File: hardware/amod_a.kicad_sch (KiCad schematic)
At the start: 50 parts, among them J101 USB-C, J102 rails, J201 SMA, J202 SMA, J301 SMA, J302 SMA, Q201 AO3401A, Q301 AO3401A, SW201 ON, SW301 ON, U101 LM2664, U102 3.3V, U201 OPA810, U301 OPA810

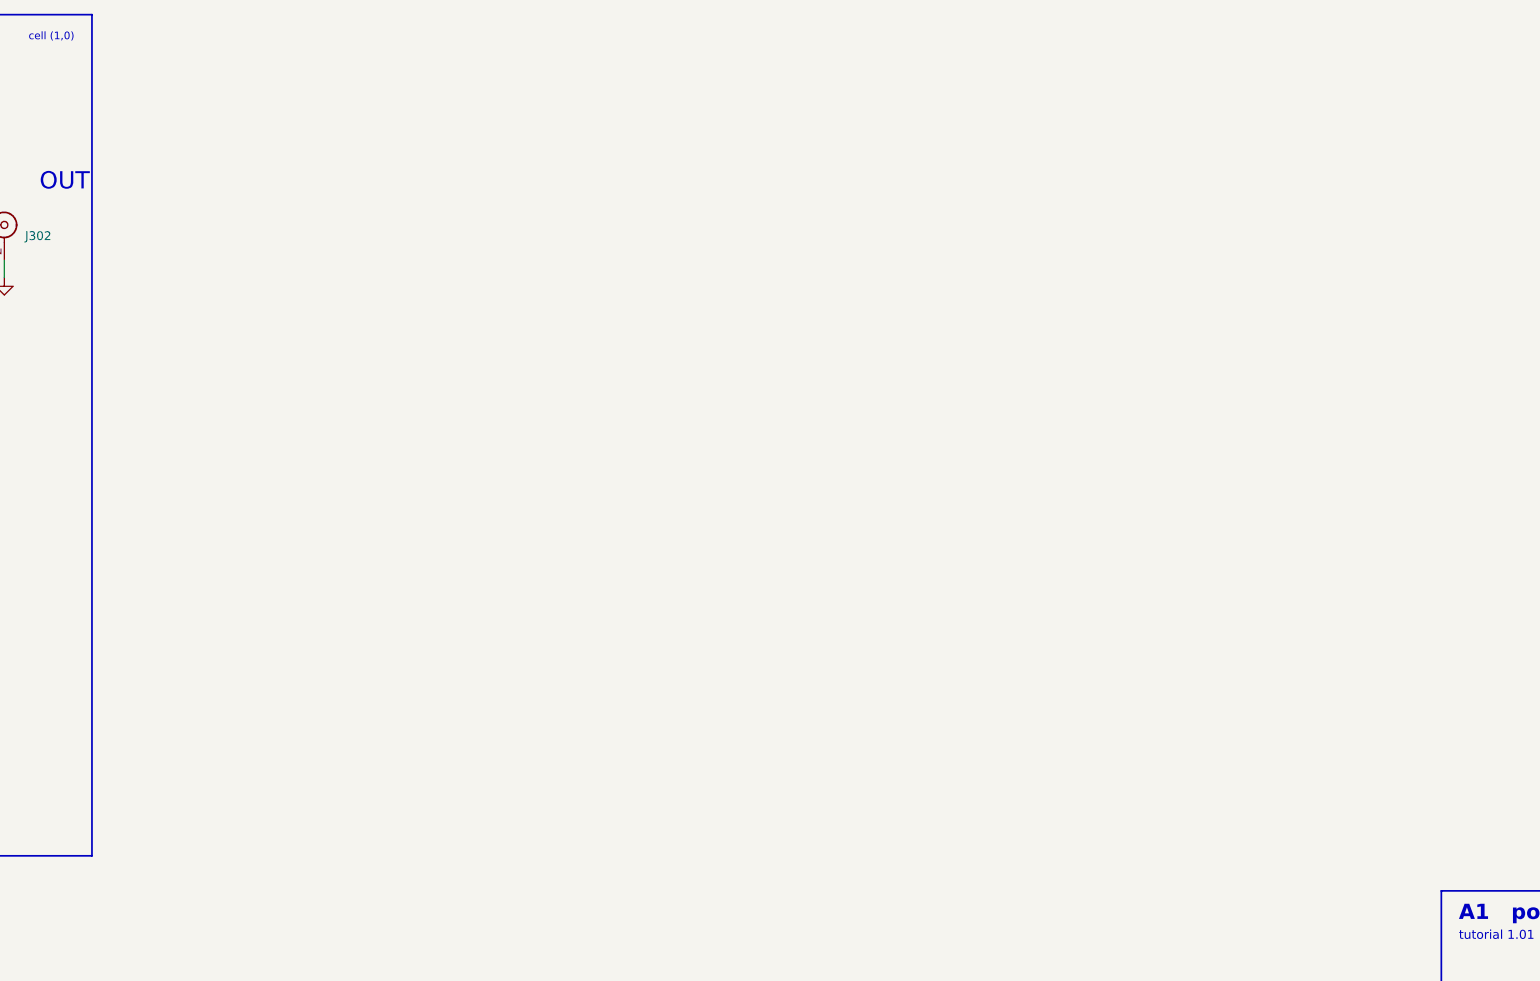
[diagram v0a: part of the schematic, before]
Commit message: AMOD-A A4: the OPA847 LNA at DRC 0 (feedback through the NC pin, VS on the back, own SOIC-8 symbol)
Co-Authored-By: Claude Fable 5.1 <noreply@anthropic.com>
Claude-Session: https://claude.ai/code/session_01RKeoKvFFzjk3cEBLCXXHnB
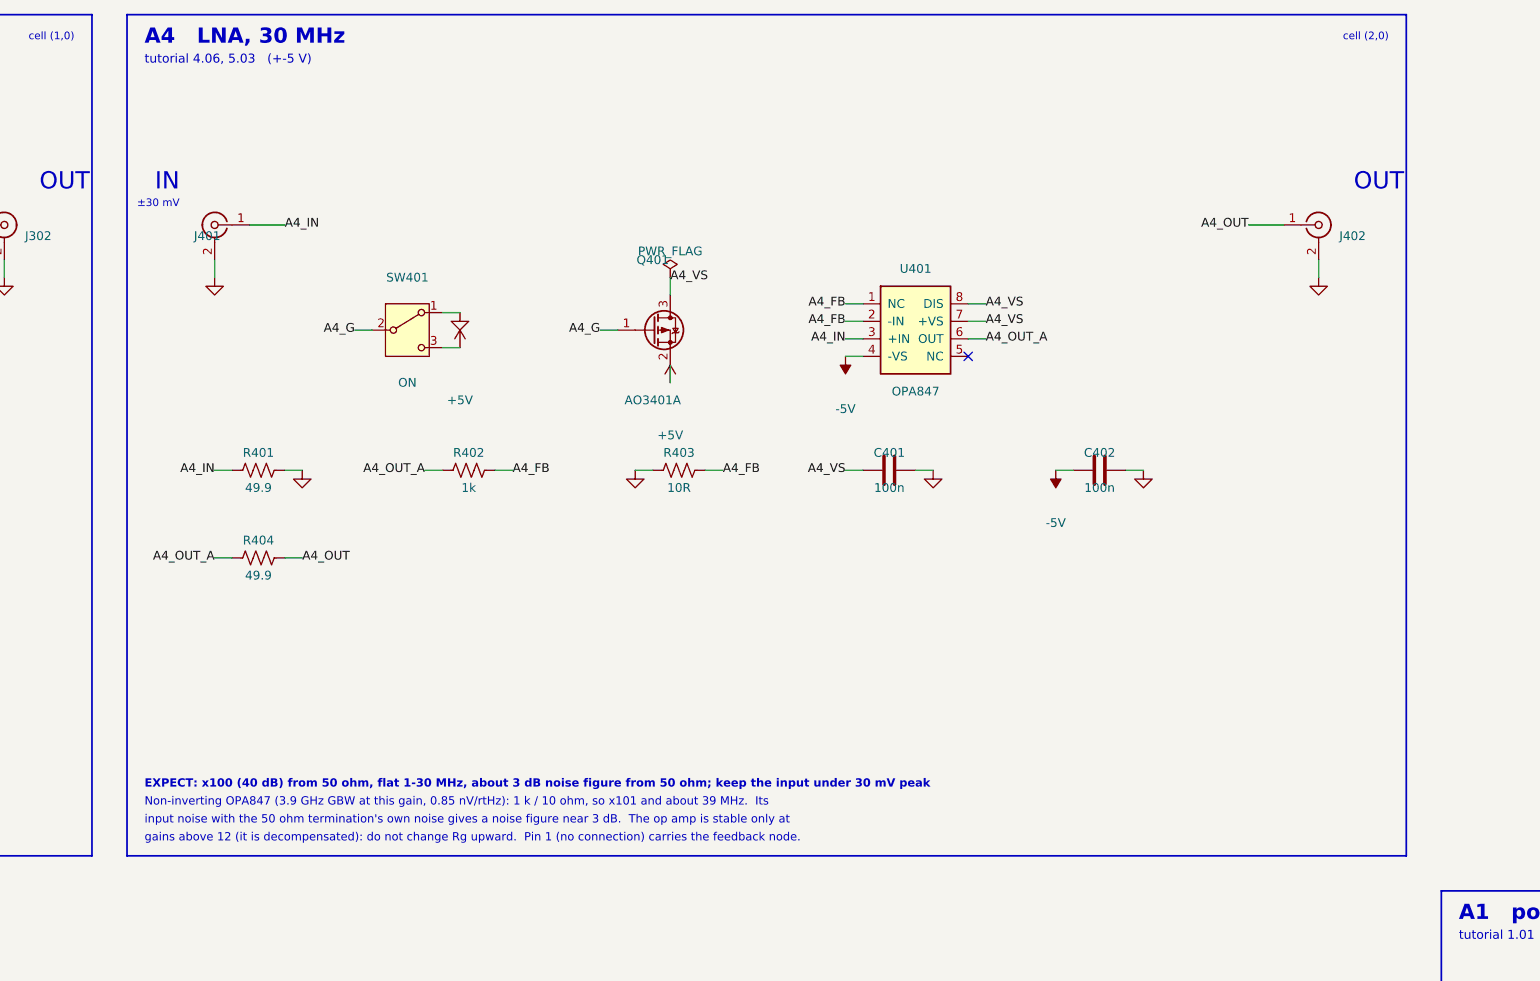
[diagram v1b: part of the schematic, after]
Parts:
- added C401, C402: 100n, Capacitor_SMD:C_0805_2012Metric, symbol Device:C
- added J401, J402: SMA, amod:SMA_BWSMA-KE-Z001_Vertical, symbol Connector:Conn_Coaxial
- added Q401: AO3401A, Package_TO_SOT_SMD:SOT-23, symbol Transistor_FET:AO3401A
- added R401, R404: 49.9, Resistor_SMD:R_0805_2012Metric, symbol Device:R_US
- added R402: 1k, Resistor_SMD:R_0805_2012Metric, symbol Device:R_US
- added R403: 10R, Resistor_SMD:R_0603_1608Metric, symbol Device:R_US
- added SW401: ON, amod:SW_SPDT_Shouhan_MSK12C02, symbol Switch:SW_SPDT
- added U401: OPA847, Package_SO:SOIC-8_3.9x4.9mm_P1.27mm, symbol amod:OPA847_SOIC8
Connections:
- net +5V: now also Q401.2 (S), SW401.3 (C)
- net -5V: now also C402.1, U401.4 (-VS)
- net GND: now also C401.2, C402.2, J401.2 (Ext), J402.2 (Ext), R401.2, R403.1, SW401.1 (A)
- new net A4_FB: R402.2, R403.2, U401.1 (NC), U401.2 (-IN)
- new net A4_G: Q401.1 (G), SW401.2 (B)
- new net A4_IN: J401.1 (In), R401.1, U401.3 (+IN)
- new net A4_OUT: J402.1 (In), R404.2
- new net A4_OUT_A: R402.1, R404.1, U401.6 (OUT)
- new net A4_VS: C401.1, Q401.3 (D), U401.7 (+VS), U401.8 (DIS)
- no-connect marks 7 -> 8
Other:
- note added: "A4 LNA, 30 MHz"
- note added: "EXPECT: x100 (40 dB) from 50 ohm, flat 1-30 MHz, about 3 dB noise figure from 50 ohm; keep the input under 30 mV peak"
- note added: "Non-inverting OPA847 (3.9 GHz GBW at this gain, 0.85 nV/rtHz): 1 k / 10 ohm, so x101 and about 39 MHz. Its"
- note added: "cell (2,0)"
- note added: "gains above 12 (it is decompensated): do not change Rg upward. Pin 1 (no connection) carries the feedback node."
- note added: "input noise with the 50 ohm termination's own noise gives a noise figure near 3 dB. The op amp is stable only at"
- note added: "tutorial 4.06, 5.03 (+-5 V)"
- note added: "±30 mV"

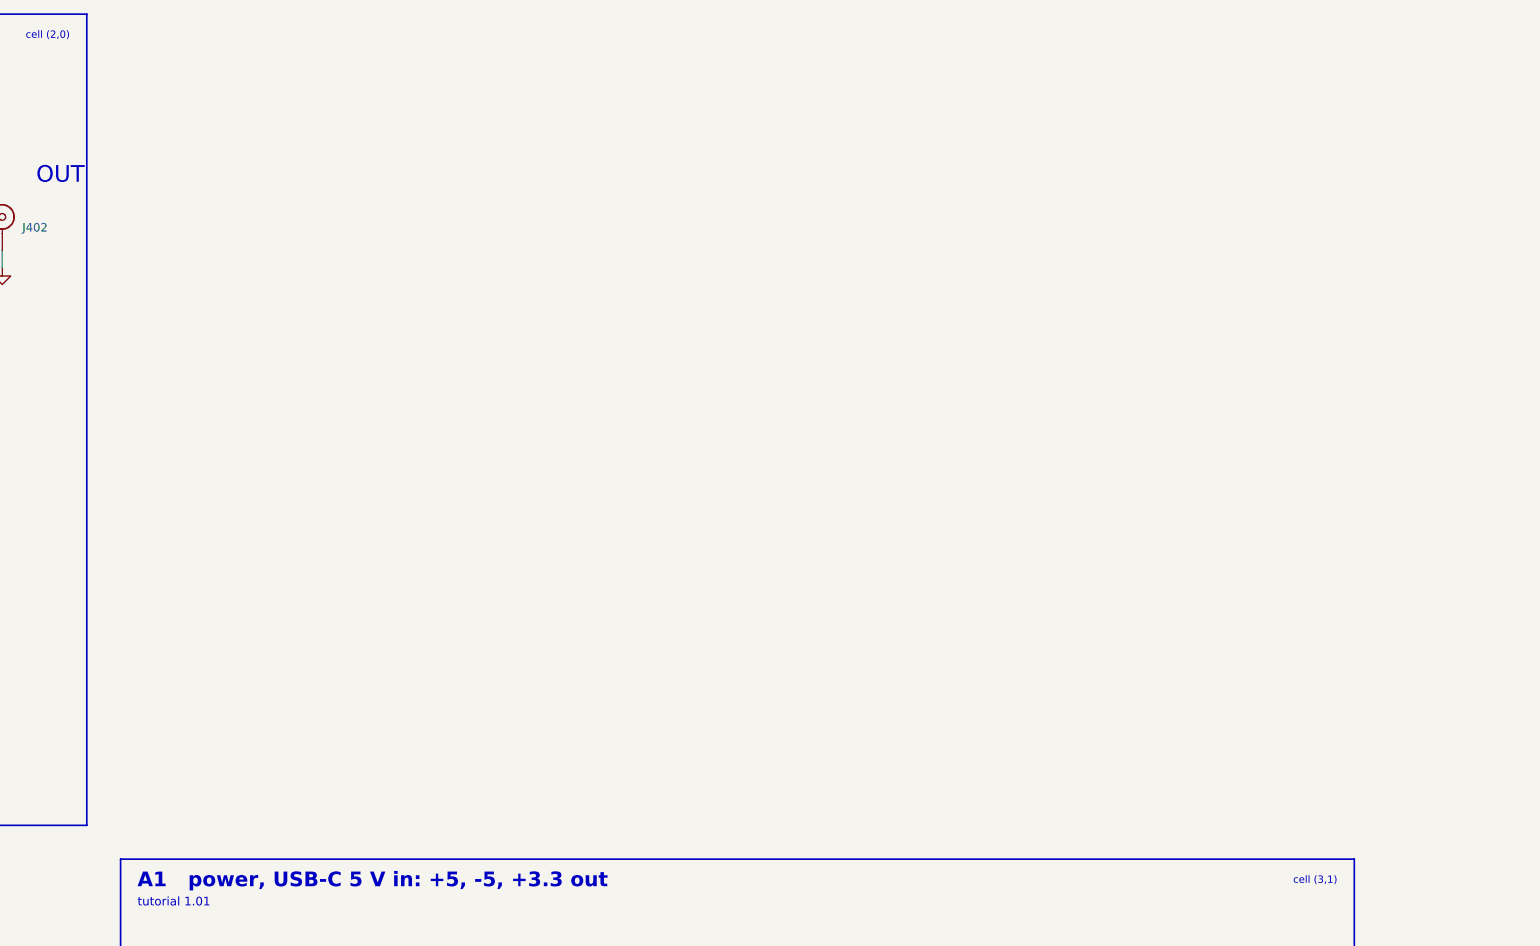
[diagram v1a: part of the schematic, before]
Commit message: AMOD-A A5: Johnson noise on an LT6230 (1.1 nV) in the A2 geometry, 10k / 1k by DIP or a socketed resistor, DRC 0
Co-Authored-By: Claude Fable 5.1 <noreply@anthropic.com>
Claude-Session: https://claude.ai/code/session_01RKeoKvFFzjk3cEBLCXXHnB
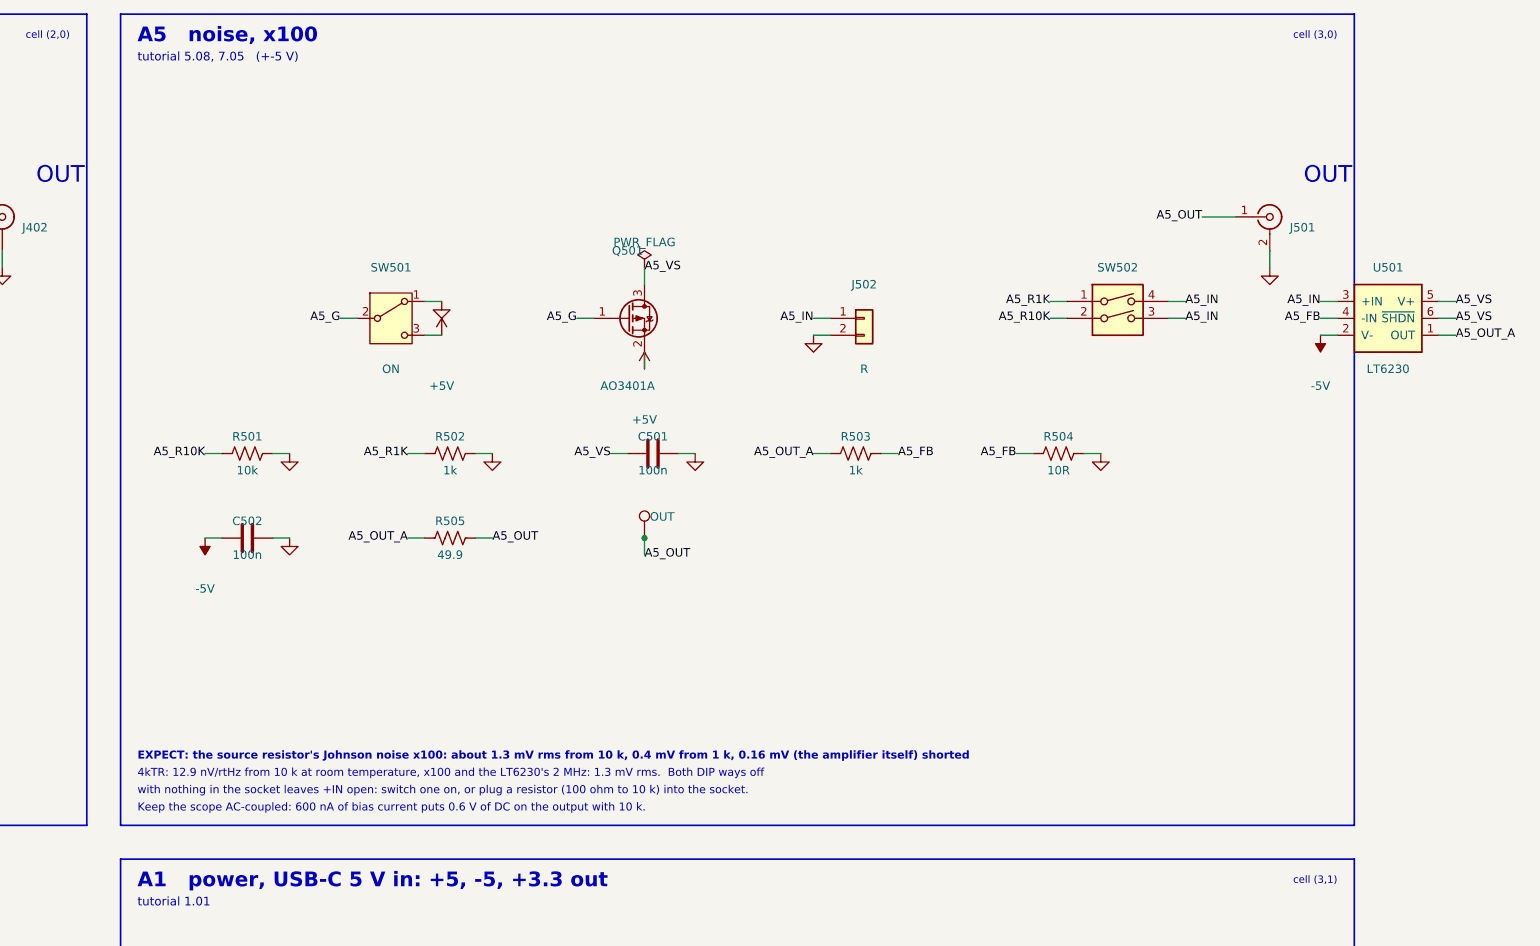
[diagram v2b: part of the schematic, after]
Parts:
- added C501, C502: 100n, Capacitor_SMD:C_0805_2012Metric, symbol Device:C
- added J501: SMA, amod:SMA_BWSMA-KE-Z001_Vertical, symbol Connector:Conn_Coaxial
- added J502: R, Connector_PinSocket_2.54mm:PinSocket_1x02_P2.54mm_Vertical, symbol Connector_Generic:Conn_01x02
- added Q501: AO3401A, Package_TO_SOT_SMD:SOT-23, symbol Transistor_FET:AO3401A
- added R501: 10k, Resistor_SMD:R_0603_1608Metric, symbol Device:R_US
- added R502: 1k, Resistor_SMD:R_0603_1608Metric, symbol Device:R_US
- added R503: 1k, Resistor_SMD:R_0805_2012Metric, symbol Device:R_US
- added R504: 10R, Resistor_SMD:R_0603_1608Metric, symbol Device:R_US
- added R505: 49.9, Resistor_SMD:R_0805_2012Metric, symbol Device:R_US
- added SW501: ON, amod:SW_SPDT_Shouhan_MSK12C02, symbol Switch:SW_SPDT
- added SW502: DIP2, amod:SW_DIP_SPSTx02_Slide_1.27mm_DSHP02, symbol Switch:SW_DIP_x02
- added TP501: OUT, amod:TestPoint_Loop_RH-5019, symbol Connector:TestPoint
- added U501: LT6230, Package_TO_SOT_SMD:SOT-23-6, symbol amod:OPA_SOT23-6
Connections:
- net +5V: now also Q501.2 (S), SW501.3 (C)
- net -5V: now also C502.1, U501.2 (V-)
- net GND: now also C501.2, C502.2, J501.2 (Ext), J502.2 (Pin_2), R501.2, R502.2, R504.2, SW501.1 (A)
- new net A5_FB: R503.2, R504.1, U501.4 (-IN)
- new net A5_G: Q501.1 (G), SW501.2 (B)
- new net A5_IN: J502.1 (Pin_1), SW502.3, SW502.4, U501.3 (+IN)
- new net A5_OUT: J501.1 (In), R505.2, TP501.1
- new net A5_OUT_A: R503.1, R505.1, U501.1 (OUT)
- new net A5_R10K: R501.1, SW502.2
- new net A5_R1K: R502.1, SW502.1
- new net A5_VS: C501.1, Q501.3 (D), U501.5 (V+), U501.6 (~{SHDN})
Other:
- note added: "4kTR: 12.9 nV/rtHz from 10 k at room temperature, x100 and the LT6230's 2 MHz: 1.3 mV rms. Both DIP ways off"
- note added: "A5 noise, x100"
- note added: "EXPECT: the source resistor's Johnson noise x100: about 1.3 mV rms from 10 k, 0.4 mV from 1 k, 0.16 mV (the amplifier itself) shorted"
- note added: "Keep the scope AC-coupled: 600 nA of bias current puts 0.6 V of DC on the output with 10 k."
- note added: "cell (3,0)"
- note added: "tutorial 5.08, 7.05 (+-5 V)"
- note added: "with nothing in the socket leaves +IN open: switch one on, or plug a resistor (100 ohm to 10 k) into the socket."

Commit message: AMOD-A A6 (delta-sigma), A8 (heater), A11 (ultrasound + the Pmod plug and lines) at DRC 0; the op-amp geometry takes an offset
- +3.3 V tiles' header via in the gutter below; board-level back wires; the QR and back text per board
- the schematic joins adjacent same-net pins with one label

Co-Authored-By: Claude Fable 5.1 <noreply@anthropic.com>
Claude-Session: https://claude.ai/code/session_01RKeoKvFFzjk3cEBLCXXHnB
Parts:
- added C1101, C1102, C801: 100n, Capacitor_SMD:C_0603_1608Metric, symbol Device:C
- added C1103, C601: 10n, Capacitor_SMD:C_0805_2012Metric, symbol Device:C
- added C1104, C1105, C602, C603: 100n, Capacitor_SMD:C_0805_2012Metric, symbol Device:C
- added J1101, J601, J801: SMA, amod:SMA_BWSMA-KE-Z001_Vertical, symbol Connector:Conn_Coaxial
- added J1102: TX, Connector_PinSocket_2.54mm:PinSocket_1x05_P2.54mm_Vertical, symbol Connector_Generic:Conn_01x05
- added J1103: RX, Connector_PinSocket_2.54mm:PinSocket_1x05_P2.54mm_Vertical, symbol Connector_Generic:Conn_01x05
- added J1104: Pmod, amod:PinHeader_2x06_P2.54mm_Horizontal_PZ254R-12-12P, symbol Connector_Generic:Conn_02x06_Odd_Even
- added Q1101, Q601, Q801: AO3401A, Package_TO_SOT_SMD:SOT-23, symbol Transistor_FET:AO3401A
- added Q802: AO3400A, Package_TO_SOT_SMD:SOT-23, symbol Transistor_FET:AO3400A
- added R1101: 3.9k, Resistor_SMD:R_0805_2012Metric, symbol Device:R_US
- added R1102, R601, R603, R604: 10k, Resistor_SMD:R_0805_2012Metric, symbol Device:R_US
- added R1103: 100R, Resistor_SMD:R_0805_2012Metric, symbol Device:R_US
- added R1104: 49.9, Resistor_SMD:R_0805_2012Metric, symbol Device:R_US
- added R602, R803: 10k, Resistor_SMD:R_0603_1608Metric, symbol Device:R_US
- added R801, R802: 15R, Resistor_SMD:R_2512_6332Metric, symbol Device:R_US
- added SW1101, SW601, SW801: ON, amod:SW_SPDT_Shouhan_MSK12C02, symbol Switch:SW_SPDT
- added TP1101: OUT, amod:TestPoint_Loop_RH-5019, symbol Connector:TestPoint
- added TP601: BIT, amod:TestPoint_Loop_RH-5019, symbol Connector:TestPoint
- added U1101: DRV8837, Package_SON:Texas_DSG0008A_WSON-8-1EP_2x2mm_P0.5mm_EP0.9x1.6mm, symbol Driver_Motor:DRV8837
- added U1102: OPA810, Package_TO_SOT_SMD:SOT-23-5, symbol amod:OPA_SOT23-5
- added U601: TLV3501, Package_TO_SOT_SMD:SOT-23-6, symbol Comparator:TLV3501AIDBV
- added U801: TMP235, Package_TO_SOT_SMD:SOT-23, symbol amod:TMP235
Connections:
- net +3V3: now also Q601.2 (S), SW601.3 (C)
- net +5V: now also Q1101.2 (S), Q801.2 (S), SW1101.3 (C), SW801.3 (C)
- net -5V: now also C1105.1, U1102.2 (V-)
- net GND: now also C1101.2, C1102.2, C1104.2, C1105.2, C601.2, C602.2, C603.2, C801.2, J1101.2 (Ext), J1103.5 (Pin_5), J1104.10 (Pin_10), J1104.9 (Pin_9), J601.2 (Ext), J801.2 (Ext), Q802.2 (S), R1101.2, R1103.2, R604.2, R803.2, SW1101.1 (A), SW601.1 (A), SW801.1 (A), U1101.4 (GND), U1101.9 (GND), U601.2 (V-), U601.6 (SHDN), U801.3 (GND)
- new net A11_FB: R1102.2, R1103.1, U1102.4 (-IN)
- new net A11_G: Q1101.1 (G), SW1101.2 (B)
- new net A11_IN: C1103.2, R1101.1, U1102.3 (+IN)
- new net A11_OUT: J1101.1 (In), R1104.2, TP1101.1
- new net A11_OUT1: J1102.1 (Pin_1), U1101.2 (OUT1)
- new net A11_OUT2: J1102.5 (Pin_5), U1101.3 (OUT2)
- new net A11_OUT_A: R1102.1, R1104.1, U1102.1 (OUT)
- new net A11_RXA: C1103.1, J1103.1 (Pin_1)
- new net A11_VS: C1101.1, C1102.1, C1104.1, Q1101.3 (D), U1101.1 (VM), U1101.7 (~{SLEEP}), U1101.8 (VCC), U1102.5 (V+)
- new net A6_G: Q601.1 (G), SW601.2 (B)
- new net A6_IN: J601.1 (In), R601.1
- new net A6_NODE: C601.1, R601.2, R602.2, U601.3 (+)
- new net A6_VREF: C603.1, R603.2, R604.1, U601.1 (-)
- new net A6_VS: C602.1, Q601.3 (D), R603.1, U601.4 (V+)
- new net A8_DRN: Q802.3 (D), R802.2
- new net A8_G: Q801.1 (G), SW801.2 (B)
- new net A8_HTR: R801.1, R802.1
- new net A8_OUT: J801.1 (In), U801.2 (VOUT)
- new net A8_VS: C801.1, Q801.3 (D), R801.2, U801.1 (VDD)
- new net PMOD1: J1104.1 (Pin_1), R602.1
- new net PMOD2: J1104.3 (Pin_3), TP601.1, U601.5
- new net PMOD3: J1104.5 (Pin_5), Q802.1 (G), R803.1
- new net PMOD5: J1104.2 (Pin_2), U1101.5 (IN2)
- new net PMOD6: J1104.4 (Pin_4), U1101.6 (IN1)
- new net PMOD_VCC: J1104.11 (Pin_11), J1104.12 (Pin_12)
- no-connect marks 8 -> 17
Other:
- note added: "10 k / 10 nF integrator (1.6 kHz; clock the loop at 1-10 MHz). IN takes 0 to 3.3 V, or +-1.5 V about the 1.65 V reference"
- note added: "A11 ultrasound"
- note added: "A6 1-bit ADC"
- note added: "A8 heat"
- note added: "Drive IN1/IN2 (Pmod 5, 6) in antiphase at 40 kHz for 8-20 cycles: the bridge puts 10 V peak to peak across the TX"
- note added: "EXPECT: 0.83 W into the board when Pmod 3 is high (the FET's drain), 10 mV/K + 500 mV on OUT"
- note added: "EXPECT: a 40 kHz burst from Pmod 5/6 leaves the TX transducer; its echo arrives x100 on RX OUT (hold a reflector over the board)"
- note added: "EXPECT: a one-bit stream on Pmod 2 whose density follows IN; the FPGA closes the loop through Pmod 1 (the handbook's gateware)"
- note added: "First-order delta-sigma: the comparator decides, the FPGA registers the bit and feeds it back through 10 k into the"
- note added: "The TMP235 reads 750 mV at 25 C and climbs 10 mV per kelvin. A feedback-control experiment: hold the TMP235 at a"
- note added: "Two 15 ohm in series: 30 ohm, 170 mA, 0.83 W from the switched 5 V when Pmod 3 is high (10 k keeps it off otherwise)."
- note added: "cell (0,1)"
- note added: "cell (2,1)"
- note added: "cells (0,3), (1,3)"
- note added: "if you AC-couple. Both Pmod lines are 3.3 V logic; the tile runs on the 3.3 V rail."
- note added: "in pins 1 and 5 (10.16 mm; their leads are 10 mm apart)."
- note added: "own resonance sets the band). Time of flight at 343 m/s: 5.8 us per mm there and back. Put the two transducers"
- note added: "set point with the FPGA's PWM. (The plan's NTC divider did not fit the cell beside the two 2512s.)"
- note added: "transducer. The RX transducer's 10 nF / 3.9 k high-pass (4 kHz) feeds an OPA810 at x100 (1.4 MHz: the transducer's"
- note added: "tutorial 4.06 (+-5 V)"
- note added: "tutorial 5.02, 7.06 (+5 V)"
- note added: "tutorial 7.05 (+3.3 V)"
- note added: "±1.5 V"
